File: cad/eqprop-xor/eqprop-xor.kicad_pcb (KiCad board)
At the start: 2 copper layers, 106 x 88 mm, 117 parts, among them J1 USB_C_Receptacle_USB2.0_14P, SW1 SW_SPDT, SW2 SW_SPDT, U1 MCP6004, U10 MCP4251-xxxx-P, U11 MCP4251-xxxx-P, U12 MCP4251-xxxx-P, U13 MCP4251-xxxx-P, U14 MCP4822, U15 MCP6002-xP, U16 ADS1115IDGS, U2 LM324, U3 Arduino_Nano_v3.x, U4 CD4053B, U5 CD4053B, U6 MCP4251-xxxx-P, U7 MCP4251-xxxx-P, U8 MCP4251-xxxx-P, U9 MCP4251-xxxx-P

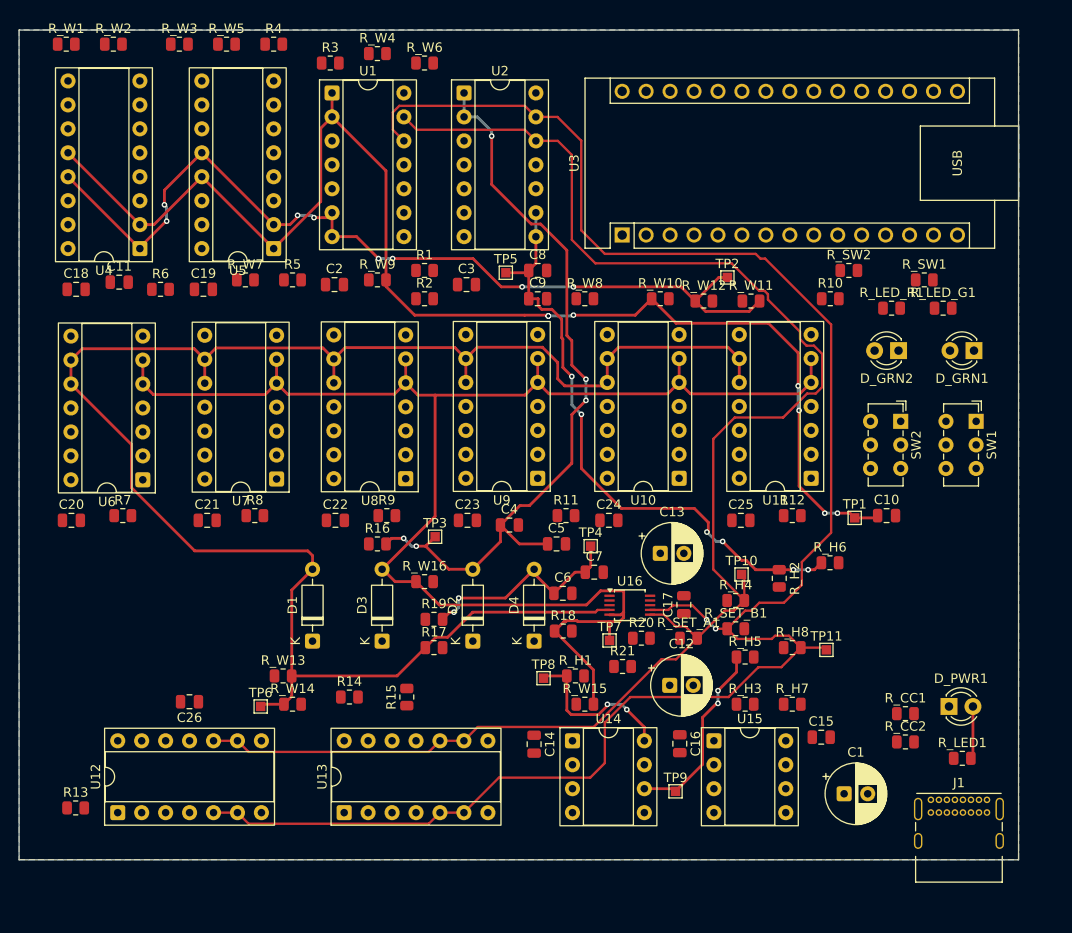
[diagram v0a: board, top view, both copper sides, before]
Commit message: Complete B.1 EqProp PCB and document fabrication and firmware handoff
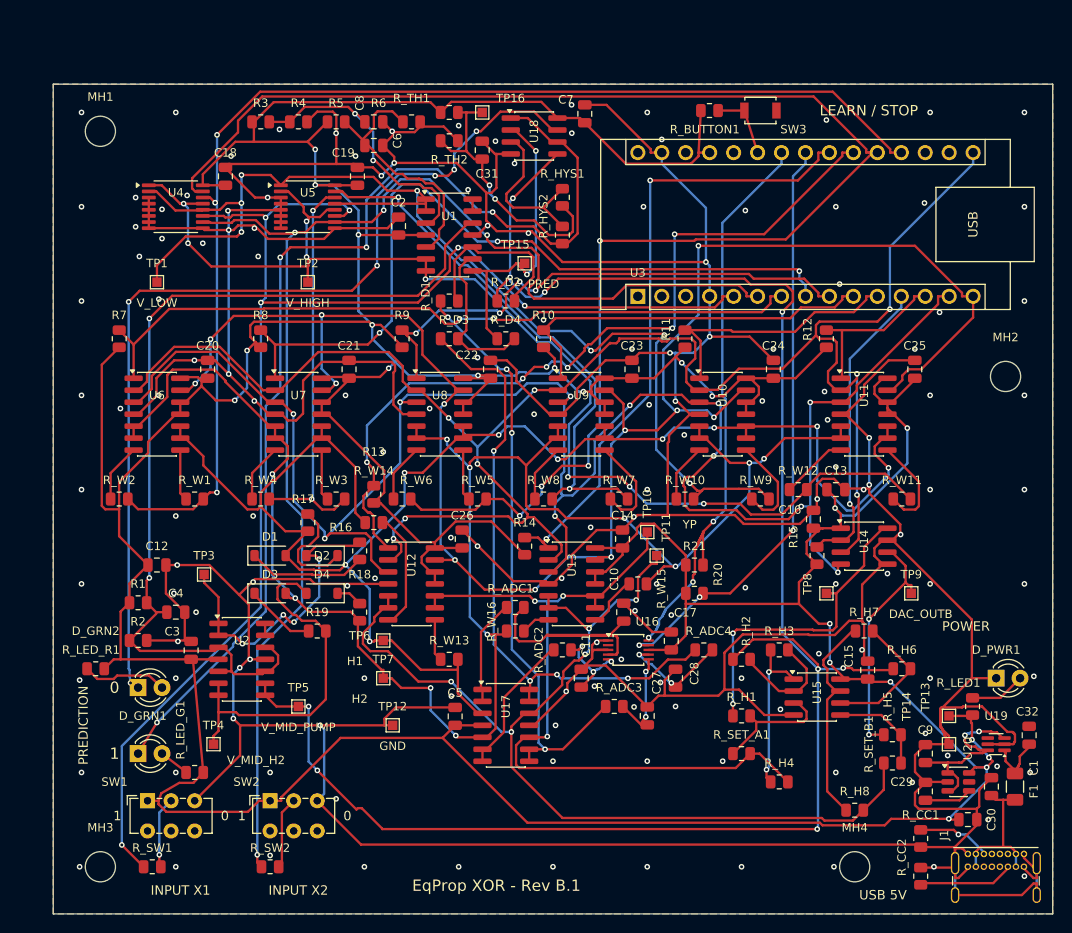
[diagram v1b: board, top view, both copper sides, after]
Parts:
- added C27: 1nF, Capacitor_SMD:C_0805_2012Metric, F.Cu at (163.0, 117.0)
- added C28: 1nF, Capacitor_SMD:C_0805_2012Metric, F.Cu at (166.0, 113.0)
- added C29: 10nF, Capacitor_SMD:C_0805_2012Metric, F.Cu at (192.5, 125.0)
- added C30: 10uF, Capacitor_SMD:C_0805_2012Metric, F.Cu at (197.0, 128.0)
- added C31: 100nF, Capacitor_SMD:C_0805_2012Metric, F.Cu at (145.5, 57.0)
- added C32: 1uF, Capacitor_SMD:C_0805_2012Metric, F.Cu at (203.5, 119.0)
- added F1: 250mA PTC, Fuse:Fuse_1206_3216Metric, F.Cu at (202.0, 124.5)
- added MH1: M3, MountingHole_3.2mm_M3, F.Cu at (105.0, 55.0)
- added MH2: M3, MountingHole_3.2mm_M3, F.Cu at (201.0, 81.0)
- added MH3: M3, MountingHole_3.2mm_M3, F.Cu at (105.0, 133.0)
- added MH4: M3, MountingHole_3.2mm_M3, F.Cu at (185.0, 133.0)
- added R_ADC1: 100, Resistor_SMD:R_0805_2012Metric, F.Cu at (149.0, 105.5)
- added R_ADC2: 100, Resistor_SMD:R_0805_2012Metric, F.Cu at (154.0, 110.0)
- added R_ADC3: 100, Resistor_SMD:R_0805_2012Metric, F.Cu at (159.5, 116.0)
- added R_ADC4: 100, Resistor_SMD:R_0805_2012Metric, F.Cu at (169.0, 110.0)
- added R_BUTTON1: 2.2k, Resistor_SMD:R_0805_2012Metric, F.Cu at (169.6, 52.8)
- added R_D1: 100k, Resistor_SMD:R_0805_2012Metric, F.Cu at (142.0, 73.0)
- added R_D2: 100k, Resistor_SMD:R_0805_2012Metric, F.Cu at (148.0, 73.0)
- added R_D3: 100k, Resistor_SMD:R_0805_2012Metric, F.Cu at (142.0, 77.0)
- added R_D4: 100k, Resistor_SMD:R_0805_2012Metric, F.Cu at (148.0, 77.0)
- added R_HYS1: 10k, Resistor_SMD:R_0805_2012Metric, F.Cu at (154.0, 62.0)
- added R_HYS2: 2M, Resistor_SMD:R_0805_2012Metric, F.Cu at (154.0, 66.0)
- added R_TH1: 4.99k, Resistor_SMD:R_0805_2012Metric, F.Cu at (142.0, 53.0)
- added R_TH2: 5.62k, Resistor_SMD:R_0805_2012Metric, F.Cu at (142.0, 56.0)
- added SW3: LEARN / STOP, Button_Switch_SMD:SW_SPST_B3U-1000P, F.Cu at (175.0, 52.8)
- added TP12: TestPoint, TestPoint:TestPoint_Pad_1.0x1.0mm, F.Cu at (136.0, 118.0)
- added TP13: TestPoint, TestPoint:TestPoint_Pad_1.0x1.0mm, F.Cu at (195.0, 117.0)
- added TP14: TestPoint, TestPoint:TestPoint_Pad_1.0x1.0mm, F.Cu at (195.0, 120.0)
- added TP15: TestPoint, TestPoint:TestPoint_Pad_1.0x1.0mm, F.Cu at (150.0, 69.0)
- added TP16: TestPoint, TestPoint:TestPoint_Pad_1.0x1.0mm, F.Cu at (145.5, 53.0)
- added U17: TLV9064IDR, Package_SO:SOIC-14_3.9x8.7mm_P1.27mm, F.Cu at (148.0, 118.0)
- added U18: TLV3202AIDR, Package_SO:SOIC-8_3.9x4.9mm_P1.27mm, F.Cu at (151.0, 55.5)
- added U19: TPS22918DBVR, Package_TO_SOT_SMD:SOT-23-6, F.Cu at (196.0, 124.0)
- added U20: LM66100DCKR, Package_TO_SOT_SMD:SOT-363_SC-70-6, F.Cu at (200.0, 120.0)
- C1: value 100µF -> 1uF; footprint Capacitor_THT:CP_Radial_D6.3mm_P2.50mm -> Capacitor_SMD:C_0805_2012Metric
- C10, C11: value 100nF -> 1nF
- C12, C13: value 100µF -> 10uF; footprint Capacitor_THT:CP_Radial_D6.3mm_P2.50mm -> Capacitor_SMD:C_0805_2012Metric
- C4, C6, C8: value 10µF -> 1uF
- C9: value 100nF -> 1uF
- D1, D2, D3, D4: value BAT42 -> BAT42W-G3-08; footprint Diode_THT:D_DO-35_SOD27_P7.62mm_Horizontal -> Diode_SMD:D_SOD-123
- D_GRN1, D_GRN2, D_PWR1: value Green 3mm -> Green low-current 3mm
- J1: footprint Connector_USB:USB_C_Receptacle_GCT_USB4085 -> EqProp:USB4085_Edge
- R1, R10, R11, R12, R13, R14, R15, R2, R7, R8, R9, R_H2, R_H6, R_SW1, R_SW2: value 10kΩ -> 10k
- R16, R17, R18, R19: value 0Ω -> 0
- R20, R21: value 4.7kΩ -> 4.7k
- R3, R6: value 33kΩ -> 33k
- R4, R5: value 8.2kΩ -> 8.2k
- R_CC1, R_CC2: value 5.1kΩ -> 5.1k
- R_H1, R_H4, R_H5, R_H8: value 10kΩ -> 1M
- R_H3, R_H7: value 10kΩ -> 20k
- R_LED1: value 1kΩ -> 1k
- R_LED_G1, R_LED_R1: value 470Ω -> 2.2k
- R_SET_A1, R_SET_B1: value 1MΩ -> 1M
- R_W1, R_W10, R_W11, R_W12, R_W13, R_W14, R_W15, R_W16, R_W2, R_W3, R_W4, R_W5, R_W6, R_W7, R_W8, R_W9: value 1.21kΩ -> 2.49k
- U1: value MCP6004 -> TLV9064IDR; footprint Package_DIP:DIP-14_W7.62mm_Socket -> Package_SO:SOIC-14_3.9x8.7mm_P1.27mm
- U10, U11, U12, U13, U6, U7, U8, U9: value MCP4251-xxxx-P -> MCP4251-104E/SL; footprint Package_DIP:DIP-14_W7.62mm_Socket -> Package_SO:SOIC-14_3.9x8.7mm_P1.27mm
- U14: value MCP4822 -> MCP4822-E/SN; footprint Package_DIP:DIP-8_W7.62mm_Socket -> Package_SO:SOIC-8_3.9x4.9mm_P1.27mm
- U15: value MCP6002-xP -> TLV9062IDR; footprint Package_DIP:DIP-8_W7.62mm_Socket -> Package_SO:SOIC-8_3.9x4.9mm_P1.27mm
- U16: value ADS1115IDGS -> ADS1115IDGSR
- U2: value LM324 -> TLV9064IDR; footprint Package_DIP:DIP-14_W7.62mm_Socket -> Package_SO:SOIC-14_3.9x8.7mm_P1.27mm
- U4, U5: value CD4053B -> TMUX1133PWR; footprint Package_DIP:DIP-16_W7.62mm_Socket -> Package_SO:TSSOP-16_4.4x5mm_P0.65mm
- moved R_SW1 102.9 mm to (110.5, 133.0)
- moved D_GRN1 98.4 mm to (109.0, 121.0), turned to 0 degrees
- moved SW1 96.7 mm to (110.0, 126.0), turned to 0 degrees
- moved R_LED_G1 93.4 mm to (115.0, 123.0)
- moved R_LED_R1 92.7 mm to (104.5, 112.0)
- moved D_GRN2 88.2 mm to (109.0, 114.0), turned to 0 degrees
- moved R_SW2 88.1 mm to (123.0, 133.0)
- moved TP1 78.1 mm to (111.0, 71.0)
- moved SW2 78.1 mm to (123.0, 126.0), turned to 0 degrees
- moved C11 64.5 mm to (156.0, 113.0), turned to 90 degrees
- moved U2 64.5 mm to (120.0, 111.0)
- moved C9 63.4 mm to (192.5, 121.0), turned to 90 degrees
- moved C12 55.9 mm to (111.0, 101.0)
- moved R_W5 55.1 mm to (145.0, 94.0)
- moved C6 53.9 mm to (134.0, 54.0)
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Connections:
- net /CS_DAC renamed CS_DAC
- net /CS_POT1 renamed CS_POT1
- net /CS_POT2 renamed CS_POT2
- net /CS_POT3 renamed CS_POT3
- net /CS_POT4 renamed CS_POT4
- net /CS_POT5 renamed CS_POT5
- net /CS_POT6 renamed CS_POT6
- net /CS_POT7 renamed CS_POT7
- net /CS_POT8 renamed CS_POT8
- net /DAC_OUTA renamed DAC_OUTA
- net /DAC_OUTB renamed DAC_OUTB
- net /I2C_SCL renamed I2C_SCL
- net /I2C_SDA renamed I2C_SDA
- net /SPI_MISO renamed SPI_MISO
- net /SPI_MOSI renamed SPI_MOSI
- net /SPI_SCK renamed SPI_SCK
- net Net-(D1-K) renamed D1_K
- net Net-(D2-K) renamed D2_K
- net Net-(D3-K) renamed D3_K
- net Net-(D4-K) renamed D4_K
- net Net-(D_GRN1-A) renamed D_GRN1_A
- net Net-(D_GRN2-A) renamed D_GRN2_A
- net Net-(D_PWR1-A) renamed D_PWR1_A
- net Net-(J1-CC1) renamed J1_CC1
- net Net-(J1-CC2) renamed J1_CC2
- net Net-(R_H3-Pad1) renamed R_H3_1
- net Net-(R_H7-Pad1) renamed R_H7_1
- net Net-(SW1-B) renamed SW1_B
- net Net-(SW2-B) renamed SW2_B
- net Net-(U10-P0A) renamed U10_P0A
- net Net-(U10-P1A) renamed U10_P1A
- net Net-(U11-P0A) renamed U11_P0A
- net Net-(U11-P1A) renamed U11_P1A
- net Net-(U12-P0A) renamed U12_P0A
- net Net-(U12-P1A) renamed U12_P1A
- net Net-(U13-P0A) renamed U13_P0A
- net Net-(U13-P1A) renamed U13_P1A
- net Net-(U15A-+) renamed U15A_P
- net Net-(U15A--) renamed U15A_N
- net Net-(U15B-+) renamed U15B_P
- net Net-(U15B--) renamed U15B_N
- net Net-(U6-P0A) renamed U6_P0A
- net Net-(U6-P1A) renamed U6_P1A
- net Net-(U7-P0A) renamed U7_P0A
- net Net-(U7-P1A) renamed U7_P1A
- net Net-(U8-P0A) renamed U8_P0A
- net Net-(U8-P1A) renamed U8_P1A
- net Net-(U9-P0A) renamed U9_P0A
- net Net-(U9-P1A) renamed U9_P1A
- C1 pad 1: +5V -> VBUS
- C10 pad 1: /V_LOW -> H1_ADC
- C11 pad 1: /V_HIGH -> H2_ADC
- C4 pad 1: /V_MID_H1 -> V_MID_RAW
- C5 pad 1: /V_MID_H1 -> +5V
- C6 pad 1: /V_MID_H2 -> V_LOW_RAW
- C7 pad 1: /V_MID_H2 -> +5V
- C8 pad 1: /V_MID_PUMP -> V_HIGH_RAW
- C9 pad 1: /V_MID_PUMP -> USB_PROTECTED
- D1 pad 2: /H1 -> H1
- D2 pad 2: /V_MID_H1 -> V_MID_H1
- D3 pad 2: /H2 -> H2
- D4 pad 2: /V_MID_H2 -> V_MID_H2
- D_GRN1 pad 1: Net-(D_GRN1-K) -> D_GRN1_K
- D_GRN2 pad 1: Net-(D_GRN2-K) -> D_GRN2_K
- J1 pad A4: +5V -> VBUS
- J1 pad A9: +5V -> VBUS
- J1 pad B4: +5V -> VBUS
- J1 pad B9: +5V -> VBUS
- R1 pad 2: /V_MID_RAW -> V_MID_RAW
- R16 pad 2: /V_MID_H1 -> V_MID_H1
- R17 pad 1: /H1 -> H1
- R18 pad 1: /H2 -> H2
- R19 pad 2: /V_MID_H2 -> V_MID_H2
- R2 pad 1: /V_MID_RAW -> V_MID_RAW
- R3 pad 2: /V_LOW_RAW -> V_LOW_RAW
- R4 pad 1: /V_LOW_RAW -> V_LOW_RAW
- R5 pad 2: /V_HIGH_RAW -> V_HIGH_RAW
- R6 pad 1: /V_HIGH_RAW -> V_HIGH_RAW
- R_H2 pad 1: /V_MID_PUMP -> V_MID_PUMP
- R_H4 pad 2: /YP -> YP
- R_H6 pad 1: /V_MID_PUMP -> V_MID_PUMP
- R_H8 pad 2: /YN -> YN
- R_SET_A1 pad 2: /YP -> YP
- R_SET_B1 pad 1: /YN -> YN
- R_SW1 pad 1: /MUX_A -> MUX_A
- R_SW2 pad 1: /MUX_B -> MUX_B
- R_W1 pad 2: /X1 -> X1
- R_W10 pad 1: /V_LOW -> V_LOW
- R_W11 pad 2: /V_HIGH -> V_HIGH
- R_W12 pad 1: /V_HIGH -> V_HIGH
- R_W13 pad 2: /H1 -> H1
- R_W14 pad 1: /H1 -> H1
- R_W15 pad 2: /H2 -> H2
- R_W16 pad 1: /H2 -> H2
- R_W2 pad 1: /X1 -> X1
- R_W3 pad 2: /X1_COMP -> X1_COMP
- R_W4 pad 1: /X1_COMP -> X1_COMP
- R_W5 pad 2: /X2 -> X2
- R_W6 pad 1: /X2 -> X2
- R_W7 pad 2: /X2_COMP -> X2_COMP
- R_W8 pad 1: /X2_COMP -> X2_COMP
- R_W9 pad 2: /V_LOW -> V_LOW
- TP1 pad 1: /V_LOW -> V_LOW
- TP10 pad 1: /YP -> YP
- TP11 pad 1: /YN -> YN
- TP2 pad 1: /V_HIGH -> V_HIGH
- TP3 pad 1: /V_MID_H1 -> V_MID_H1
- TP4 pad 1: /V_MID_H2 -> V_MID_H2
- TP5 pad 1: /V_MID_PUMP -> V_MID_PUMP
- TP6 pad 1: /H1 -> H1
- TP7 pad 1: /H2 -> H2
- U1 pad 1: /V_LOW -> V_LOW
- U1 pad 10: GND -> PRED_PLUS
- U1 pad 12: /YN -> V_MID_RAW
- U1 pad 13: /YP -> PARK_U1
- U1 pad 14: Net-(D_GRN1-K) -> PARK_U1
- U1 pad 2: /V_LOW -> V_LOW
- U1 pad 3: /V_LOW_RAW -> V_LOW_RAW
- U1 pad 5: /V_HIGH_RAW -> V_HIGH_RAW
- U1 pad 6: /V_HIGH -> V_HIGH
- U1 pad 7: /V_HIGH -> V_HIGH
- U1 pad 8: Net-(U1C--) -> PRED
- U1 pad 9: Net-(U1C--) -> PRED_MINUS
- U10 pad 10: /H1 -> H1
- U10 pad 5: /H2 -> H2
- U10 pad 6: /H2 -> H2
- U10 pad 9: /H1 -> H1
- U11 pad 10: /H1 -> H1
- U11 pad 5: /H2 -> H2
- U11 pad 6: /H2 -> H2
- U11 pad 9: /H1 -> H1
- U12 pad 10: /YP -> YP
- U12 pad 5: /YN -> YN
- U12 pad 6: /YN -> YN
- U12 pad 9: /YP -> YP
- U13 pad 10: /YP -> YP
- U13 pad 5: /YN -> YN
- U13 pad 6: /YN -> YN
- U13 pad 9: /YP -> YP
- U16 pad 4: /H1 -> H1_ADC
- U16 pad 5: /H2 -> H2_ADC
- U16 pad 6: /YP -> YP_ADC
- U16 pad 7: /YN -> YN_ADC
- U2 pad 1: /V_MID_H1 -> V_MID_H1
- U2 pad 10: /V_MID_RAW -> V_MID_RAW
- U2 pad 12: /YP -> V_MID_RAW
- U2 pad 13: /YN -> PARK_U2
- U2 pad 14: Net-(D_GRN2-K) -> PARK_U2
- U2 pad 2: /V_MID_H1 -> V_MID_H1
- U2 pad 3: /V_MID_RAW -> V_MID_RAW
- U2 pad 5: /V_MID_RAW -> V_MID_RAW
- U2 pad 6: /V_MID_H2 -> V_MID_H2
- U2 pad 7: /V_MID_H2 -> V_MID_H2
- U2 pad 8: /V_MID_PUMP -> V_MID_PUMP
- U2 pad 9: /V_MID_PUMP -> V_MID_PUMP
- U3 pad 19: /X1 -> X1
- U3 pad 20: /X2 -> X2
- U3 pad 25: unconnected-(U3-A6-Pad25) -> LEARN_BUTTON
- U3 pad 5: /MUX_A -> MUX_A
- U3 pad 6: /MUX_B -> MUX_B
- U4 pad 1: /V_HIGH -> V_HIGH
- U4 pad 10: /X2 -> MUX_B
- U4 pad 11: /X1 -> MUX_A
- U4 pad 12: /V_LOW -> V_LOW
- U4 pad 13: /V_HIGH -> V_HIGH
- U4 pad 14: /MUX_A -> X1
- U4 pad 15: /MUX_B -> X2
- U4 pad 2: /V_LOW -> V_LOW
- U5 pad 1: /V_LOW -> V_LOW
- U5 pad 10: /X2_COMP -> MUX_B
- U5 pad 11: /X1_COMP -> MUX_A
- U5 pad 12: /V_HIGH -> V_HIGH
- U5 pad 13: /V_LOW -> V_LOW
- U5 pad 14: /MUX_A -> X1_COMP
- U5 pad 15: /MUX_B -> X2_COMP
- U5 pad 2: /V_HIGH -> V_HIGH
- U6 pad 10: /H1 -> H1
- U6 pad 5: /H2 -> H2
- U6 pad 6: /H2 -> H2
- U6 pad 9: /H1 -> H1
- U7 pad 10: /H1 -> H1
- U7 pad 5: /H2 -> H2
- U7 pad 6: /H2 -> H2
- U7 pad 9: /H1 -> H1
- U8 pad 10: /H1 -> H1
- U8 pad 5: /H2 -> H2
- U8 pad 6: /H2 -> H2
- U8 pad 9: /H1 -> H1
- U9 pad 10: /H1 -> H1
- U9 pad 5: /H2 -> H2
- U9 pad 6: /H2 -> H2
- U9 pad 9: /H1 -> H1
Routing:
- net GND: track 0.00 -> 742.7 mm, vias 0 -> 151
- net +5V: track 0.00 -> 609.5 mm, vias 0 -> 21
- net SPI_MOSI: track 0.00 -> 200.1 mm, vias 0 -> 11
- net V_MID_PUMP: track 0.00 -> 198.7 mm, vias 0 -> 9
- net /YN: track 198.4 -> 0.00 mm, vias 2 -> 0
- net SPI_SCK: track 0.00 -> 195.4 mm, vias 0 -> 8
- net SPI_MISO: track 0.00 -> 193.2 mm, vias 0 -> 12
- net H2: track 0.00 -> 189.0 mm, vias 0 -> 11
- net /H1: track 185.4 -> 0.00 mm
- net /YP: track 169.0 -> 0.00 mm
- net H1: track 0.00 -> 168.7 mm, vias 0 -> 9
- net /H2: track 163.7 -> 0.00 mm
- net X2: track 0.00 -> 162.4 mm, vias 0 -> 4
- net MUX_A: track 0.00 -> 151.4 mm, vias 0 -> 6
- net MUX_B: track 0.00 -> 144.0 mm, vias 0 -> 4
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- added copper zone on F.Cu, net GND
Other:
- board text added: "0"
- board text added: "1"
- board text added: "Analog equilibrium: free phase <-> nudged phase"
- board text added: "Complementary paths represent signed weights."
- board text added: "DAC_OUTB"
- board text added: "EqProp XOR - Rev B.1"
- board text added: "EqProp XOR | circuit guide"
- board text added: "GND"
- board text added: "H1"
- board text added: "H1 H2 Diode activation"
- board text added: "H2"
- board text added: "HIDDEN NODES"
- board text added: "INPUT MUXES"
- board text added: "INPUT X1"
- board text added: "INPUT X2"
- board text added: "LEARN / STOP"
- board text added: "Links: programmable resistances (weight pots)"
- board text added: "Nano measures node changes and updates pot settings."
- board text added: "OUTPUT NODES"
- board text added: "POWER"
- board text added: "PRED"
- board text added: "PREDICTION"
- board text added: "Prediction LEDs show class, not training status."
- board text added: "SW3: learn / stop (firmware required)"
- board text added: "USB 5V"
- board text added: "V_HIGH"
- board text added: "V_LOW"
- board text added: "V_MID_H2"
- board text added: "V_MID_PUMP"
- board text added: "X1 / X1 complement X2 / X2 complement"
- board text added: "XOR: 00 -> 0 01 -> 1 10 -> 1 11 -> 0"
- board text added: "YP"
- board text added: "YP YN Readout: YP - YN"
